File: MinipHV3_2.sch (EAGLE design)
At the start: 35 parts, among them IC1 MCP3221, IC4 LMP7702, IC5 TPS60400DBV

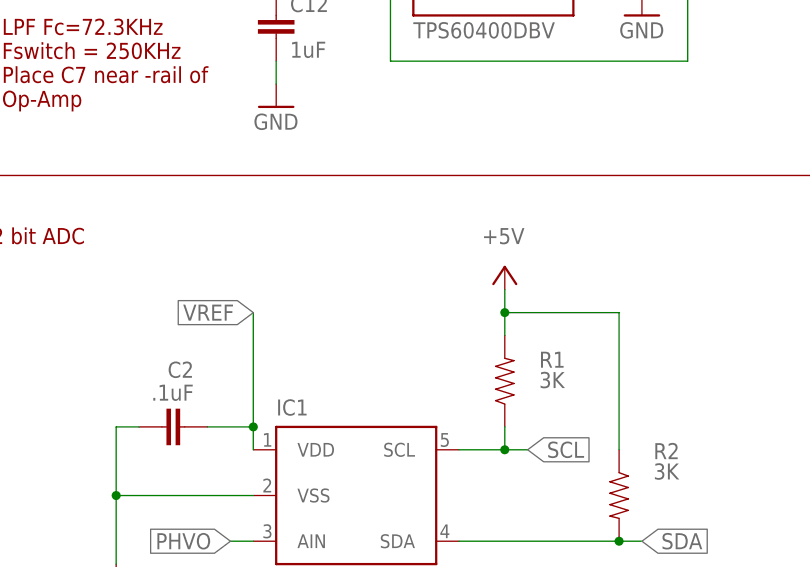
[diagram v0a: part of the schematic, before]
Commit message: added in bridge jumper VCC to Vref
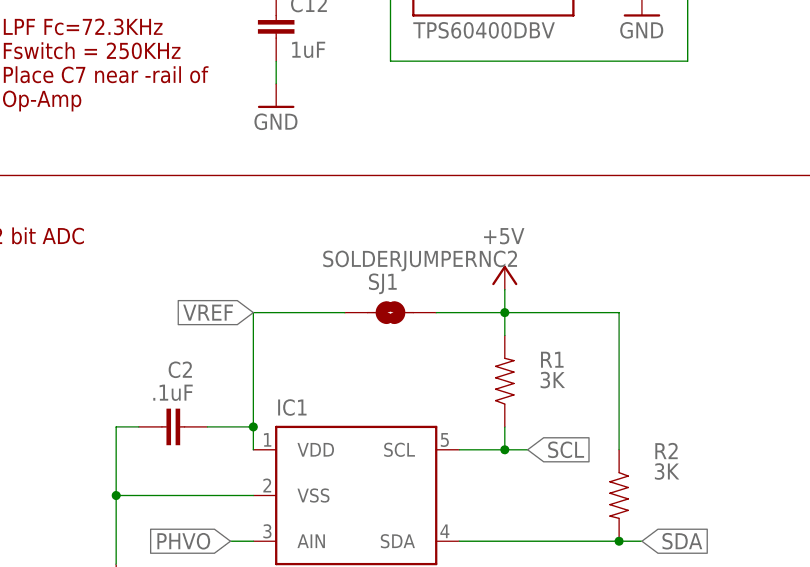
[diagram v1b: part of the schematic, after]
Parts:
- added SJ1: SOLDERJUMPERNC2, SparkFun:SOLDERJUMPERNC2
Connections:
- net +5V: now also SJ1.2
- net VREF: now also SJ1.1
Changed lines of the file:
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@@
 <part name="P+4" library="supply1" deviceset="+5V" device=""/>
 <part name="GND2" library="supply1" deviceset="GND" device=""/>
+<part name="SJ1" library="SparkFun" deviceset="SOLDERJUMPER" device="NC2"/>
 </parts>
 <sheets>
@@
 <attribute name="VALUE" x="127" y="149.86" size="1.778" layer="96"/>
 </instance>
+<instance part="SJ1" gate="1" x="210.82" y="106.68" smashed="yes">
+<attribute name="NAME" x="208.28" y="109.22" size="1.778" layer="95"/>
+<attribute name="VALUE" x="203.2" y="111.76" size="1.778" layer="96"/>
+</instance>
 </instances>
 <busses>
@@
 <pinref part="R2" gate="G$1" pin="1"/>
 <wire x1="223.52" y1="106.68" x2="236.22" y2="106.68" width="0.1524" layer="91"/>
+<pinref part="SJ1" gate="1" pin="2"/>
+<wire x1="223.52" y1="106.68" x2="215.9" y2="106.68" width="0.1524" layer="91"/>
 </segment>
 <segment>
@@
 <junction x="195.58" y="93.98"/>
 <label x="195.58" y="106.68" size="1.778" layer="95" rot="R180" xref="yes"/>
-</segment>
-<segment>
+<pinref part="SJ1" gate="1" pin="1"/>
+<wire x1="195.58" y1="106.68" x2="205.74" y2="106.68" width="0.1524" layer="91"/>
+</segment>
+<segment>
